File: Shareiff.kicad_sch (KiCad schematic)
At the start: 3 parts, among them J1 USB_A, U1 STM32WBA65RIV6

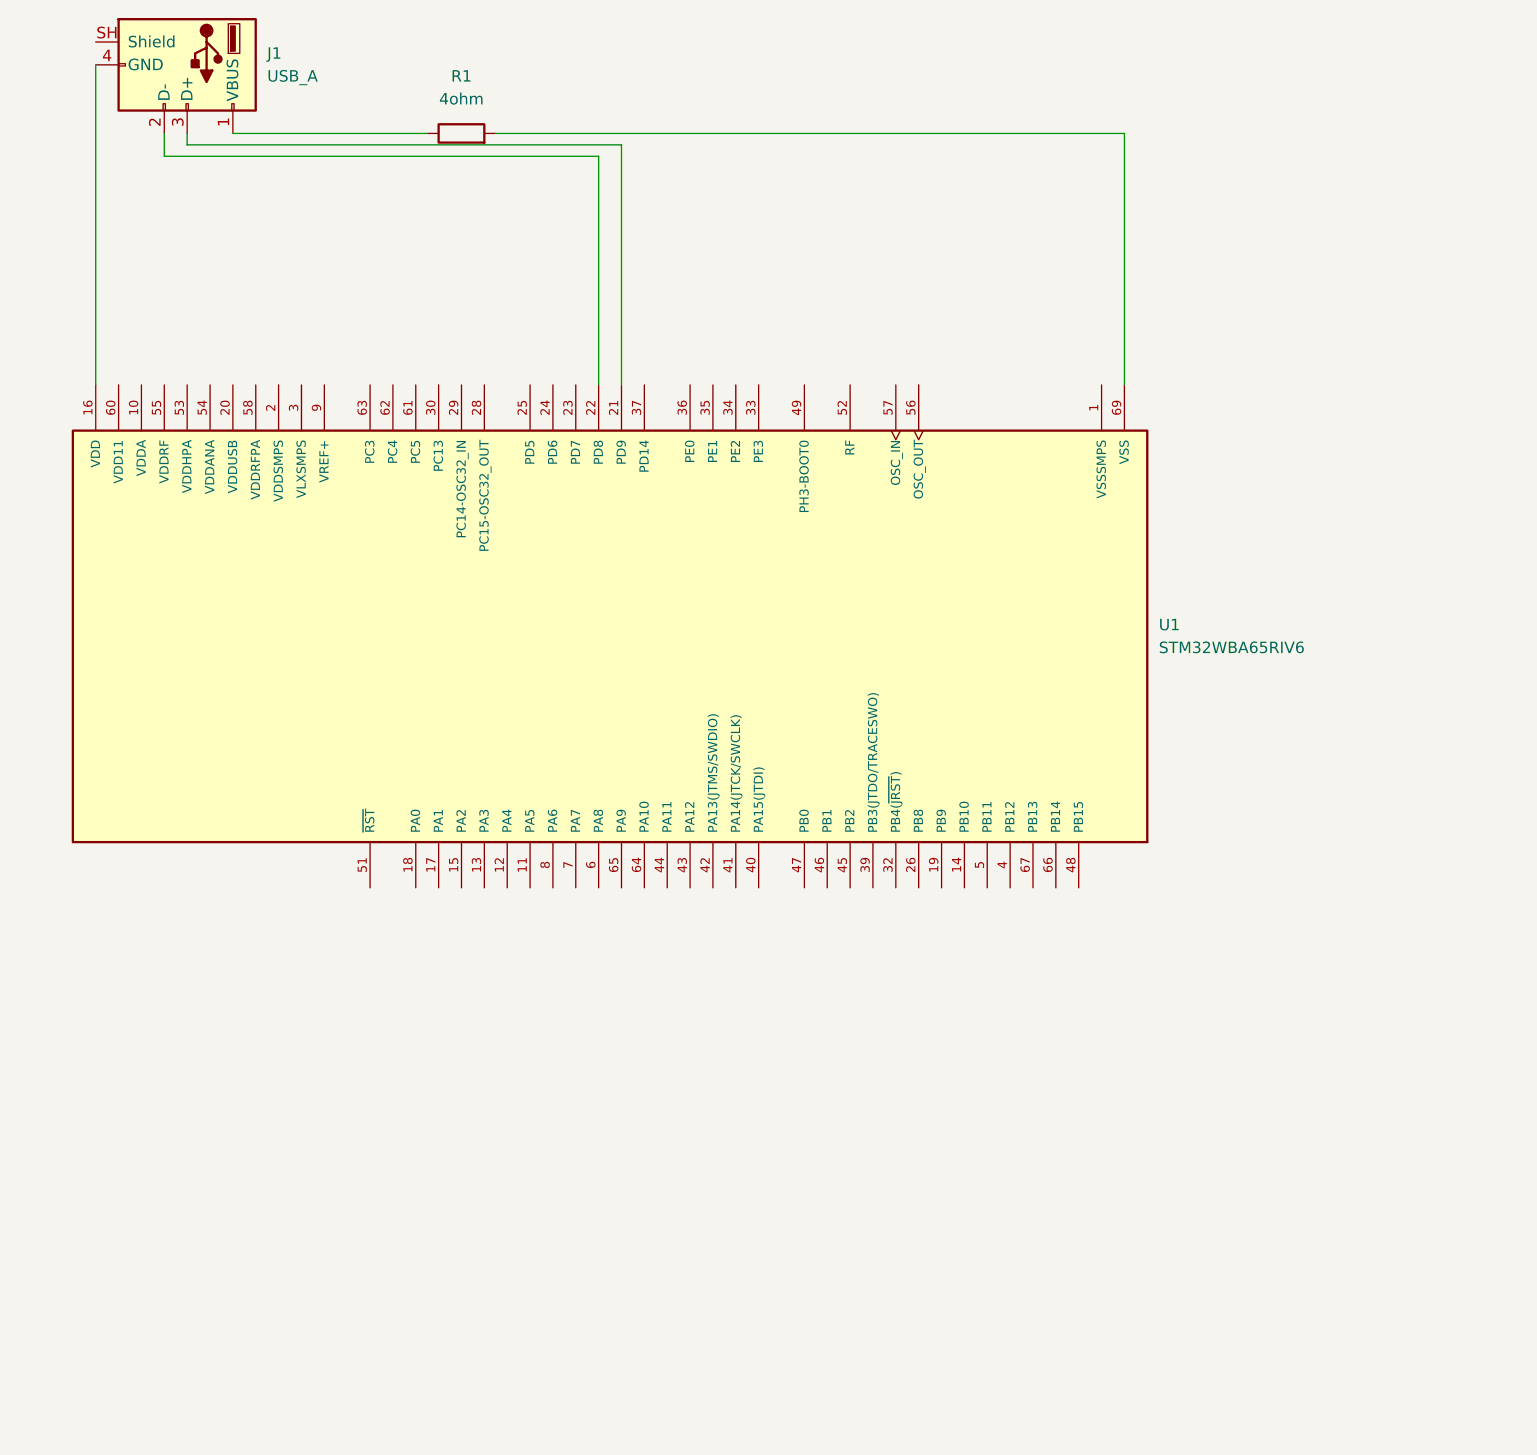
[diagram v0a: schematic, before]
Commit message: Added reset switch
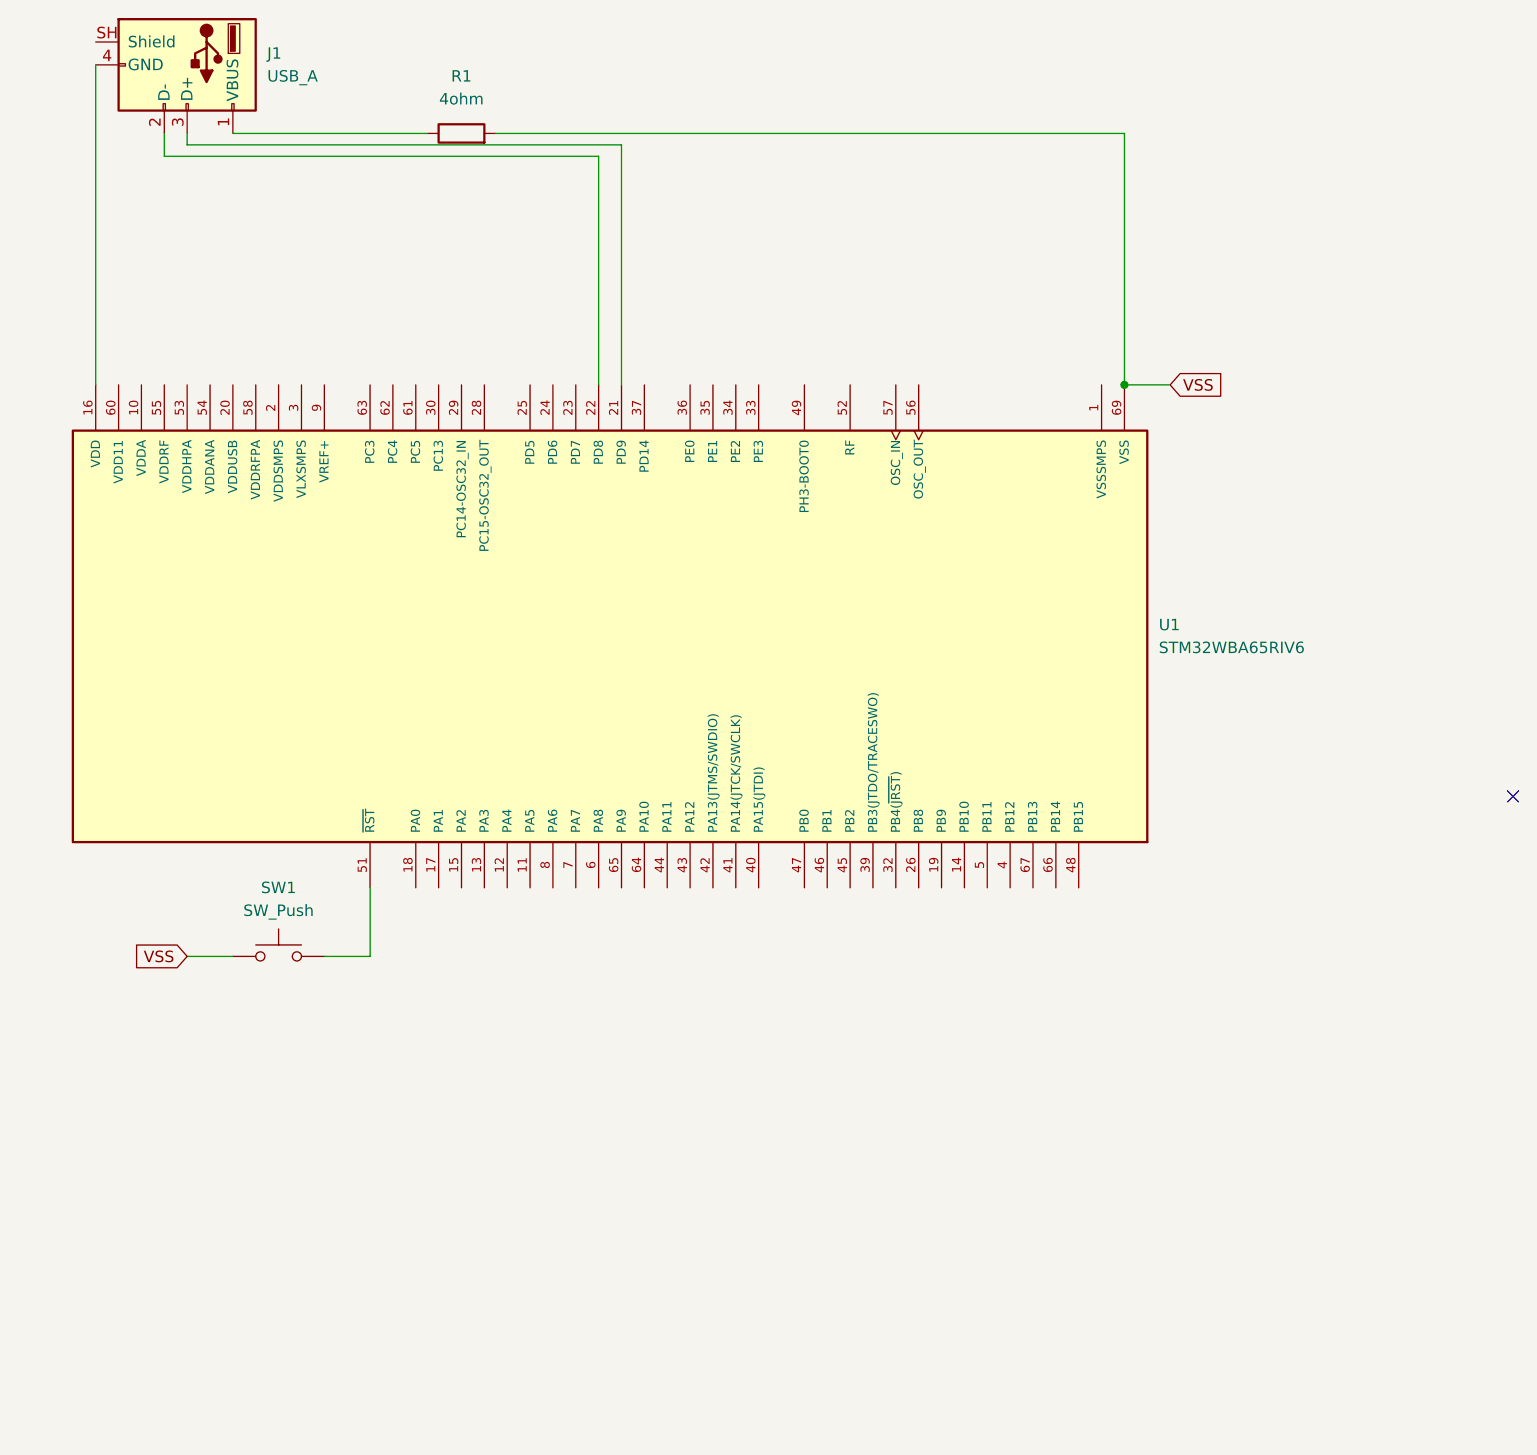
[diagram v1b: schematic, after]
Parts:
- added SW1: SW_Push, symbol Switch:SW_Push
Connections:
- net VSS: now reaches R1.2, U1.69 (VSS)
- net VSS: now also SW1.1
- net at U1.51 (~{RST}): now also SW1.2
- no-connect marks 0 -> 1
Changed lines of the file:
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@@
 	(generator_version "10.0")
 	(paper "A4")
+	(junction
+		(at 138.43 78.74)
+		(diameter 0)
+		(color 0 0 0 0)
+	)
+	(no_connect
+		(at 181.61 124.46)
+	)
 	(wire
 		(pts
@@
 	(wire
 		(pts
+			(xy 54.61 142.24) (xy 49.53 142.24)
+		)
+		(stroke
+			(width 0)
+			(type default)
+		)
+	)
+	(wire
+		(pts
+			(xy 54.61 134.62) (xy 54.61 142.24)
+		)
+		(stroke
+			(width 0)
+			(type default)
+		)
+	)
+	(wire
+		(pts
 			(xy 138.43 50.8) (xy 138.43 78.74)
 		)
@@
 			(width 0)
 			(type default)
+		)
+	)
+	(wire
+		(pts
+			(xy 138.43 78.74) (xy 143.51 78.74)
+		)
+		(stroke
+			(width 0)
+			(type default)
+		)
+	)
+	(wire
+		(pts
+			(xy 34.29 142.24) (xy 39.37 142.24)
+		)
+		(stroke
+			(width 0)
+			(type default)
+		)
+	)
+	(global_label "VSS"
+		(shape input)
+		(at 34.29 142.24 180)
+		(fields_autoplaced yes)
+		(effects
+			(font
+				(size 1.27 1.27)
+			)
+			(justify right)
+		)
+		(property "Intersheetrefs" "${INTERSHEET_REFS}"
+			(at 27.7972 142.24 0)
+			(hide yes)
+			(show_name no)
+			(do_not_autoplace no)
+			(effects
+				(font
+					(size 1.27 1.27)
+				)
+				(justify right)
+			)
+		)
+	)
+	(global_label "VSS"
+		(shape input)
+		(at 143.51 78.74 0)
+		(fields_autoplaced yes)
+		(effects
+			(font
+				(size 1.27 1.27)
+			)
+			(justify left)
+		)
+		(property "Intersheetrefs" "${INTERSHEET_REFS}"
+			(at 150.0028 78.74 0)
+			(hide yes)
+			(show_name no)
+			(do_not_autoplace no)
+			(effects
+				(font
+					(size 1.27 1.27)
+				)
+				(justify left)
+			)
 		)
 	)
@@
 					(unit 1)
 				)
+			)
+		)
+	)
+	(symbol
+		(lib_id "Switch:SW_Push")
+		(at 44.45 142.24 0)
+		(unit 1)
+		(body_style 1)
+		(exclude_from_sim no)
+		(in_bom yes)
+		(on_board yes)
+		(in_pos_files yes)
+		(dnp no)
+		(fields_autoplaced yes)
+		(property "Reference" "SW1"
+			(at 44.45 134.62 0)
+			(show_name no)
+			(do_not_autoplace no)
+			(effects
+				(font
+					(size 1.27 1.27)
+				)
+			)
+		)
+		(property "Value" "SW_Push"
+			(at 44.45 137.16 0)
+			(show_name no)
+			(do_not_autoplace no)
+			(effects
+				(font
+					(size 1.27 1.27)
+				)
+			)
+		)
+		(property "Footprint" ""
+			(at 44.45 137.16 0)
+			(hide yes)
+			(show_name no)
+			(do_not_autoplace no)
+			(effects
+				(font
+					(size 1.27 1.27)
+				)
+			)
+		)
+		(property "Datasheet" ""
+			(at 44.45 137.16 0)
+			(hide yes)
+			(show_name no)
+			(do_not_autoplace no)
+			(effects
+				(font
+					(size 1.27 1.27)
+				)
+			)
+		)
+		(property "Description" "Push button switch, generic, two pins"
+			(at 44.45 142.24 0)
+			(hide yes)
+			(show_name no)
+			(do_not_autoplace no)
+			(effects
+				(font
+					(size 1.27 1.27)
+				)
+			)
+		)
+		(pin "2"
+		)
+		(pin "1"
+		)
+		(instances
+			(project "Shareiff"
+				(path "/040ec991-b6bb-43d7-bdda-70d709947ea8"
+					(reference "SW1")
+					(unit 1)
+				)

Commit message: Uhh I forgor
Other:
- note added: "Off board connector (diag)"

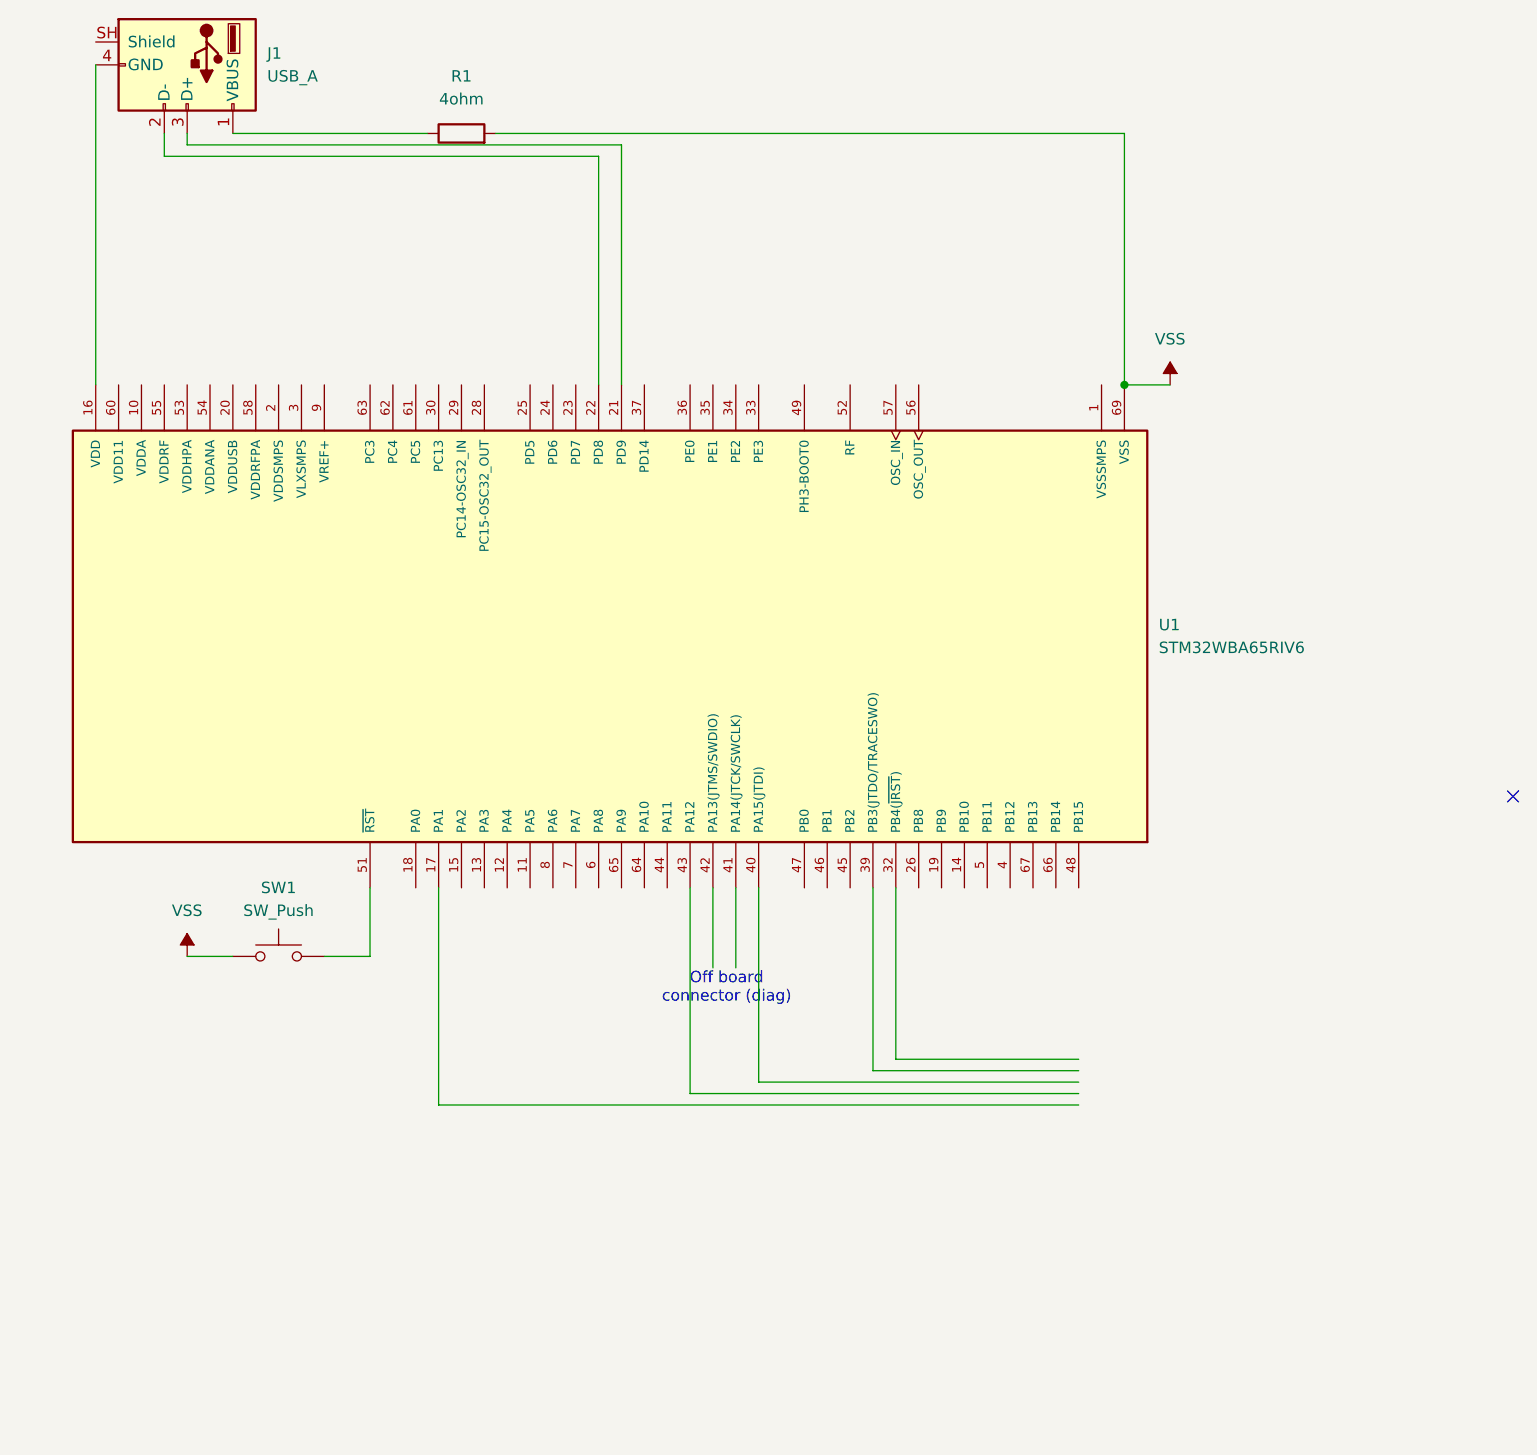
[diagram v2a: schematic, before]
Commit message: Wired Display
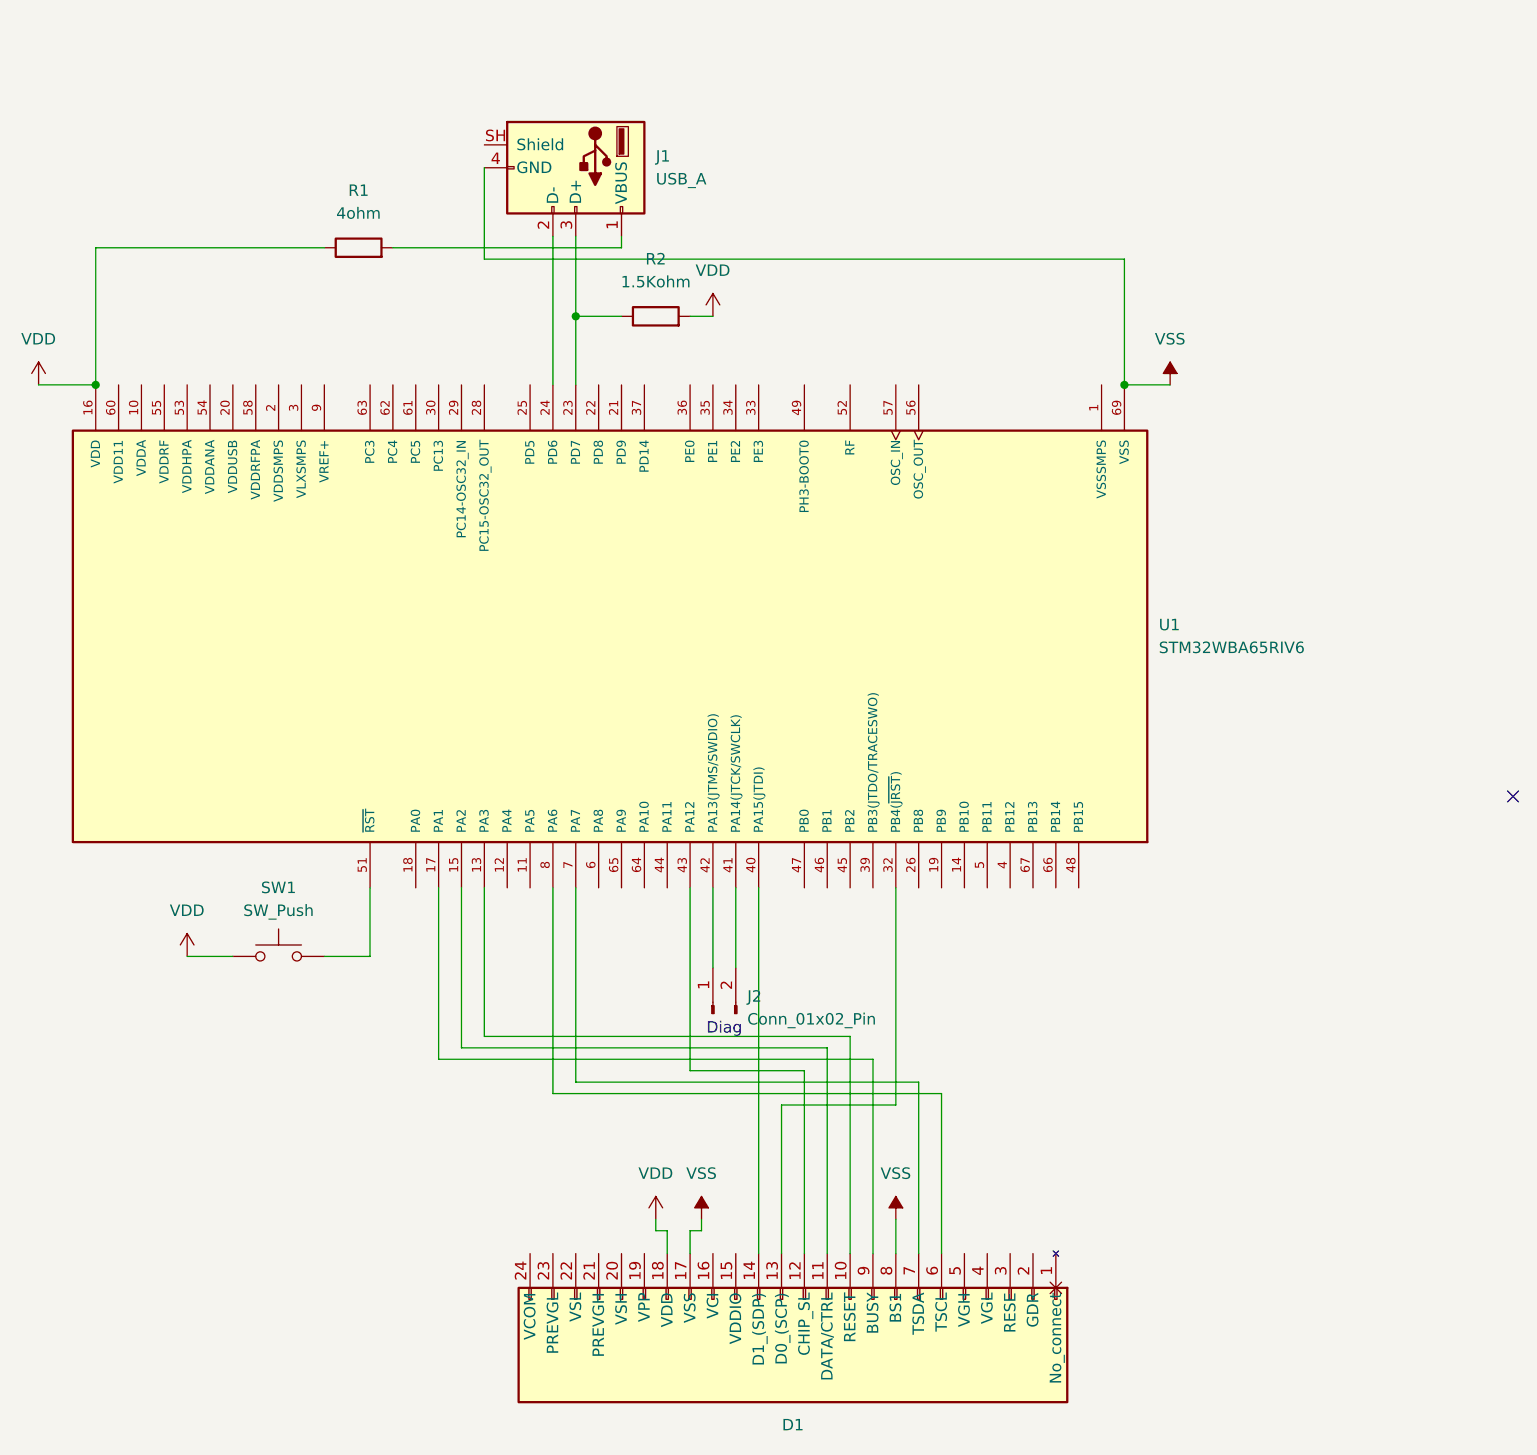
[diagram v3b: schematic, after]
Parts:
- added D1: (no value), Package_TO_SOT_SMD:SOT-583-8, symbol GOODDISPLAY-GDEW029I6FD:GDEW029I6FD
- added J2: Conn_01x02_Pin, Connector:Tag-Connect_TC2030-IDC-FP_2x03_P1.27mm_Vertical, symbol Connector:Conn_01x02_Pin
- added R2: 1.5Kohm, symbol Device:R
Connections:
- net VDD: now also R1.1, SW1.1, D1.18 (VDD), R2.2; no longer J1.4 (GND)
- net VSS: now also J1.4 (GND), D1.17 (VSS), D1.8 (BS1); no longer R1.2, SW1.1
- net at J1.1 (VBUS): now also R1.2; no longer R1.1
- net at J1.2 (D-): now also U1.24 (PD6); no longer U1.22 (PD8)
- net at J1.3 (D+): now also U1.23 (PD7), R2.1; no longer U1.21 (PD9)
- net at U1.13 (PA3): now also D1.10 (RESET)
- net at U1.15 (PA2): now also D1.11 (DATA/CTRL)
- net at U1.17 (PA1): now also D1.9 (BUSY)
- net at U1.32 (PB4(~{JRST})): now also D1.13 (D0_(SCP))
- net at U1.40 (PA15(JTDI)): now also D1.14 (D1_(SDP))
- net at U1.41 (PA14(JTCK/SWCLK)): now also J2.2 (Pin_2)
- net at U1.42 (PA13(JTMS/SWDIO)): now also J2.1 (Pin_1)
- net at U1.43 (PA12): now also D1.12 (CHIP_SL)
- net at U1.7 (PA7): now also D1.7 (TSDA)
- net at U1.8 (PA6): now also D1.6 (TSCL)
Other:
- note added: "Diag"
- note removed: "Off board connector (diag)"
- moved on the sheet: J1, R1
